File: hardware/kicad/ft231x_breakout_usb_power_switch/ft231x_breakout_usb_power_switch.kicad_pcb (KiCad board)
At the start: 2 copper layers, 60 x 31.2 mm, 71 parts, among them J1 USB_B_Micro_ALT, J2 USB_A_ALT, J3 Conn_01x08, J4 Conn_01x06, J5 Conn_01x08, Q3 2N7002, SW1 B3U-1000P, U1 SRV05-4, U2 FT231XS, U3 TPS2553DBVR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

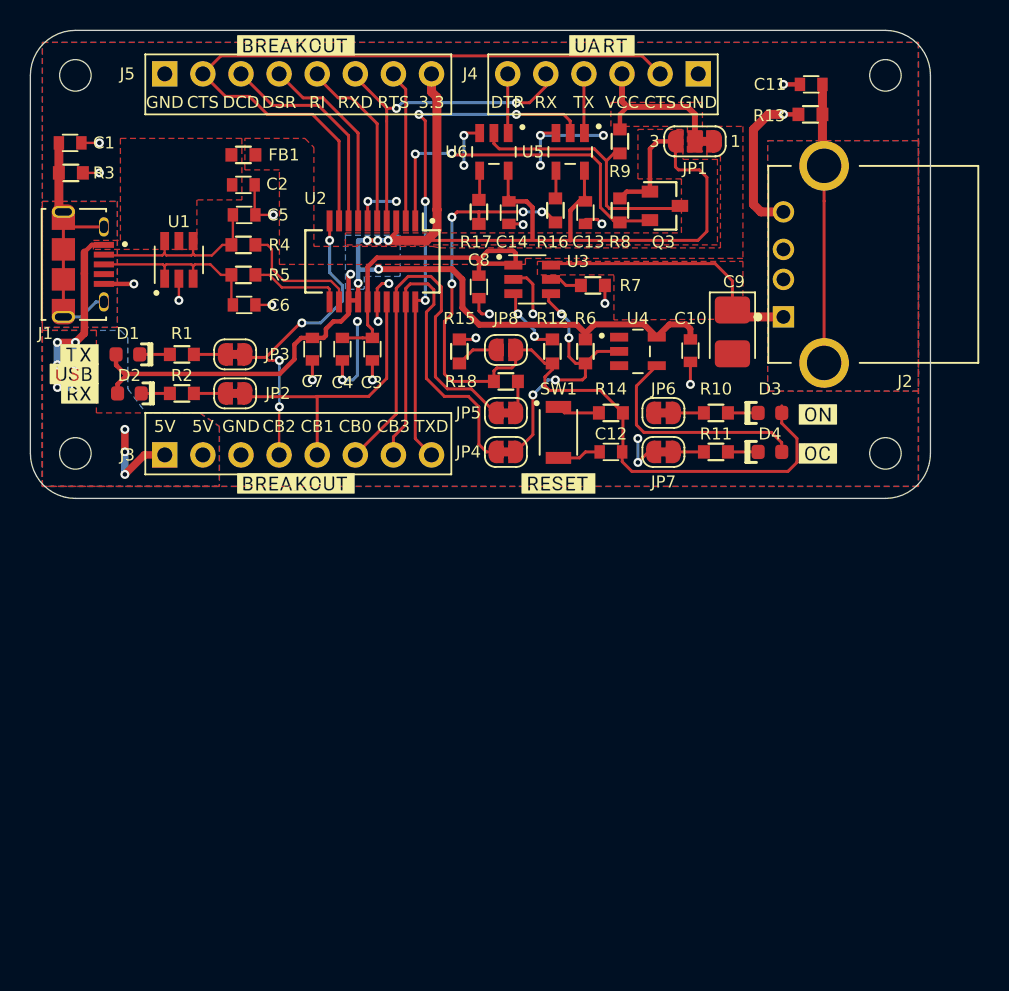
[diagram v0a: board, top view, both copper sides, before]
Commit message: Add two fiducials
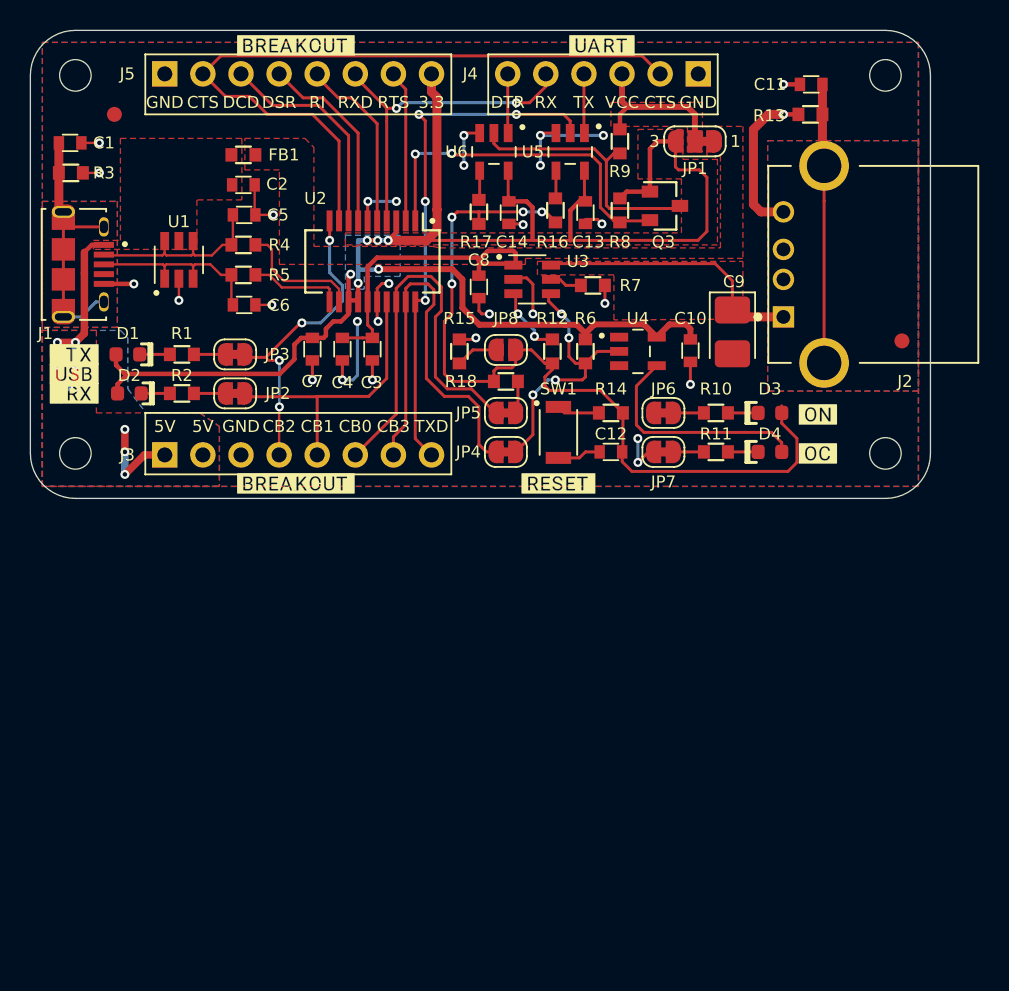
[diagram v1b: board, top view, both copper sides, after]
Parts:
- added FID1: Fiducial, -Mechanical:Fiducial_1mm_Mask2mm, F.Cu at (115.6, 75.0)
- added FID2: Fiducial, -Mechanical:Fiducial_1mm_Mask2mm, F.Cu at (168.1, 90.1)
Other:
- board text added: "VCC UART is 5V, to change to 3.3V cut JP1 pads 1 & 2 and bridge JP1 pads 2 & 3."
- board text removed: "VOUT UART is 5V, to change to 3.3V cut JP1 pads 1 & 2 and bridge JP1 pads 2 & 3."

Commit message: update resistor values in enable line
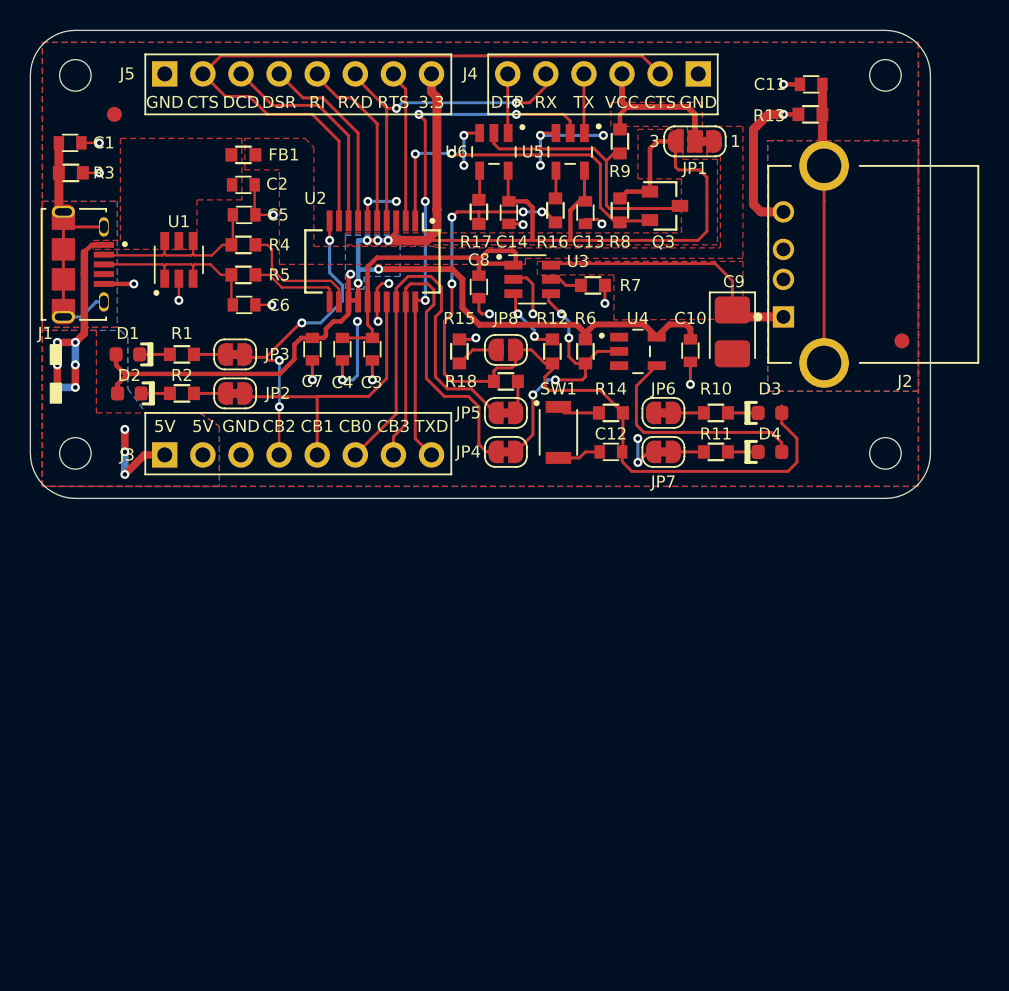
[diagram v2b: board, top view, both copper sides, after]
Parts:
- removed ? (x9): , buzzard_labels

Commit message: remove breakout headers and simplify
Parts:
- removed C14: 0.1uF, -Passive:C_0603
- removed J3: Conn_01x08, -Connector:PinHeader_1x08_P2.54mm_Vertical_CBUS
- removed J5: Conn_01x08, -Connector:PinHeader_1x08_P2.54mm_Vertical_CTS
- removed JP1: SolderJumper_3_Bridged12, -Switch:SolderJumper-3_P1.3mm_Bridged12_RoundedPad1.0x1.5mm_NumberLabels
- removed JP2, JP3, JP4, JP5, JP6, JP7: SolderJumper_2_Bridged_Alt, -Switch:SolderJumper-2_P1.3mm_Bridged_RoundedPad1.0x1.5mm
- removed Q3: 2N7002, -Chip:SOT-23-3
- removed R12, R16, R17: 1k, -Passive:R_0603
- removed R8, R9: 10k, -Passive:R_0603
- removed U6: NC7SZ66M5X, -Chip:SOT-23-5
- J4: value Conn_01x06 -> Conn_01x04; footprint -Connector:PinHeader_1x06_P2.54mm_Vertical_Arduino -> -Connector:PinHeader_1x04_P2.54mm_Vertical_Arduino
- R15: value 1k -> 10k
- R18: value 10k -> 1k
- moved J4 15.6 mm to (139.1, 74.8)
- moved U5 3.90 mm to (143.5, 80.5)
- moved D1 1.40 mm to (117.9, 91.0)
- moved D2 1.40 mm to (118.0, 93.6)
- moved R1 1.40 mm to (121.5, 91.0)
- moved R2 1.40 mm to (121.5, 93.6)
- moved C13 0.55 mm to (147.0, 81.0), turned to 90 degrees
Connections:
- net +5V renamed Net-(C3-Pad1)
- net VBUS renamed Net-(C2-Pad1)
- J4 pad 1: GND -> +3V3
- J4 pad 2: /CTS -> /STXD
- J4 pad 3: /VOUT -> /RXD
- J4 pad 4: /STXD -> GND
- R1 pad 1: Net-(JP3-Pad1) -> /TXLED
- R10 pad 1: Net-(JP6-Pad1) -> GND
- R11 pad 2: Net-(JP7-Pad1) -> GND
- R18 pad 2: Net-(JP5-Pad1) -> /GPO
- R2 pad 1: Net-(JP2-Pad1) -> /RXLED
- U2 pad 1: /DTR -> Net-(U2-Pad1)
- U2 pad 19: /GPI -> /FAULT
- U2 pad 2: /RTS -> Net-(U2-Pad2)
- U2 pad 5: /RI -> Net-(U2-Pad5)
- U2 pad 7: /DSR -> Net-(U2-Pad7)
- U2 pad 8: /DCD -> Net-(U2-Pad8)
- U2 pad 9: /CTS -> Net-(U2-Pad9)
- U3 pad 3: Net-(R12-Pad2) -> /EN
- U5 pad 4: Net-(R16-Pad2) -> /EN
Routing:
- net /CTS: track 47.9 -> 0.00 mm
- net +3V3: track 117.7 -> 86.2 mm
- net /GPI: track 28.4 -> 0.00 mm
- net /DTR: track 23.3 -> 0.00 mm, vias 2 -> 0
- net Net-(C2-Pad1): track 22.4 -> 0.00 mm, vias 9 -> 0
- net /TXD: track 35.1 -> 15.6 mm, vias 4 -> 2
- net /RES: track 18.2 -> 0.00 mm
- net /RXD: track 22.6 -> 7.37 mm, vias 2 -> 0
- net /DCD: track 14.7 -> 0.00 mm
- net /FAULT: track 18.1 -> 31.1 mm
- net /DSR: track 12.9 -> 0.00 mm
- net /RI: track 11.9 -> 0.00 mm
- net /VOUT: track 11.3 -> 0.00 mm
- net GND: track 64.8 -> 54.1 mm, vias 30 -> 23
- net /RTS: track 10.1 -> 0.00 mm
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- removed copper zone on F.Cu, net /VOUT
- removed copper zone on B.Cu, net Net-(C2-Pad1)
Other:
- board text removed: "VCC UART is 5V, to change to 3.3V cut JP1 pads 1 & 2 and bridge JP1 pads 2 & 3."

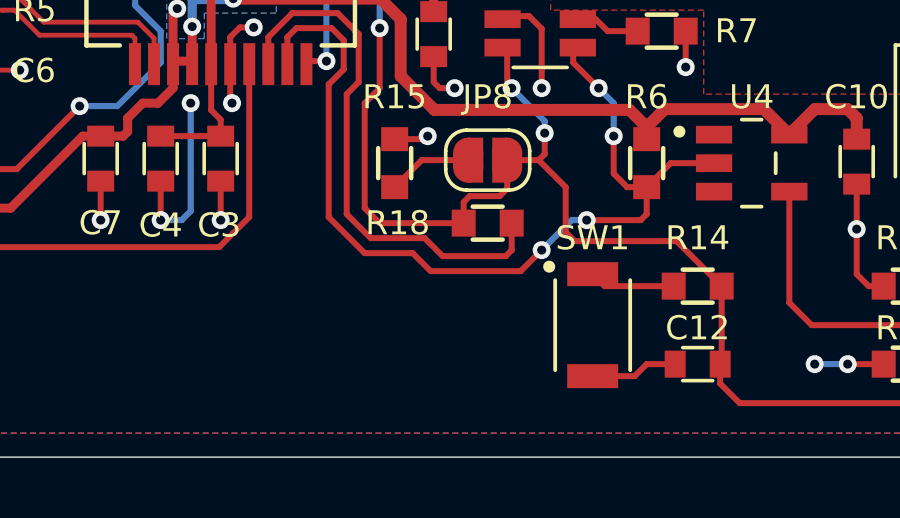
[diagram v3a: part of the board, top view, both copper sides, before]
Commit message: change to larger tactile switch
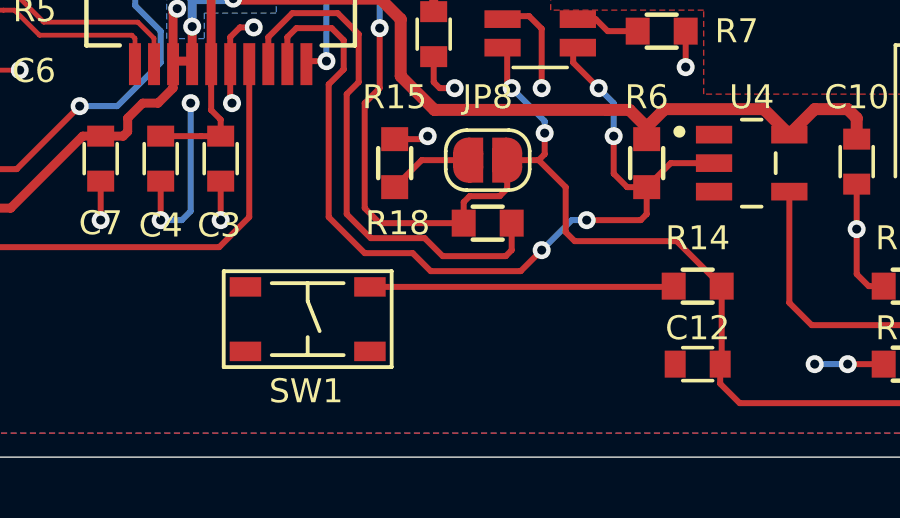
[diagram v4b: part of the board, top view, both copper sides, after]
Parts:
- SW1: value B3U-1000P -> PTS810SJK250SMTRLFS; footprint -Switch:B3U-1000P -> -Switch:PTS810SJK250SMTRLFS-TACT4.2MM
- moved SW1 9.50 mm to (135.7, 96.0), turned to 180 degrees
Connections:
- SW1 pad 1: Net-(R14-Pad1) -> GND
- SW1 pad 2: GND -> Net-(SW1-Pad2)
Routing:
- net Net-(R14-Pad1): track 2.87 -> 10.2 mm
- net GND: track 54.1 -> 51.2 mm

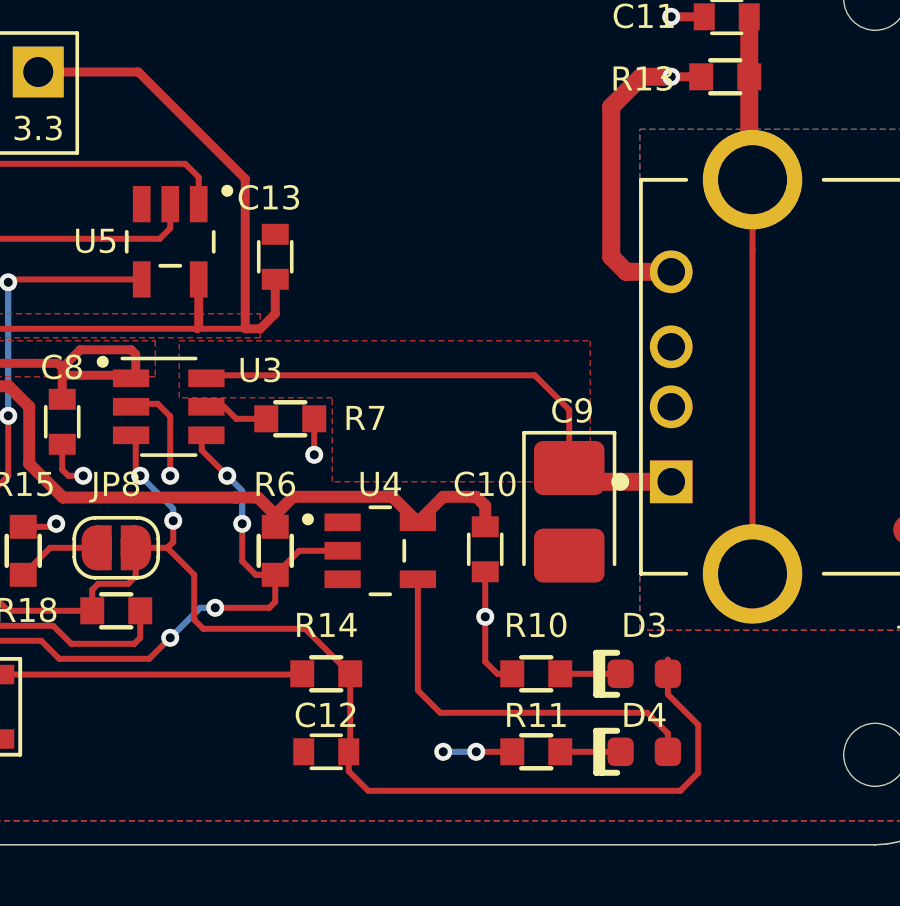
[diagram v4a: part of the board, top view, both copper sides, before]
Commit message: use buffer for on indicator
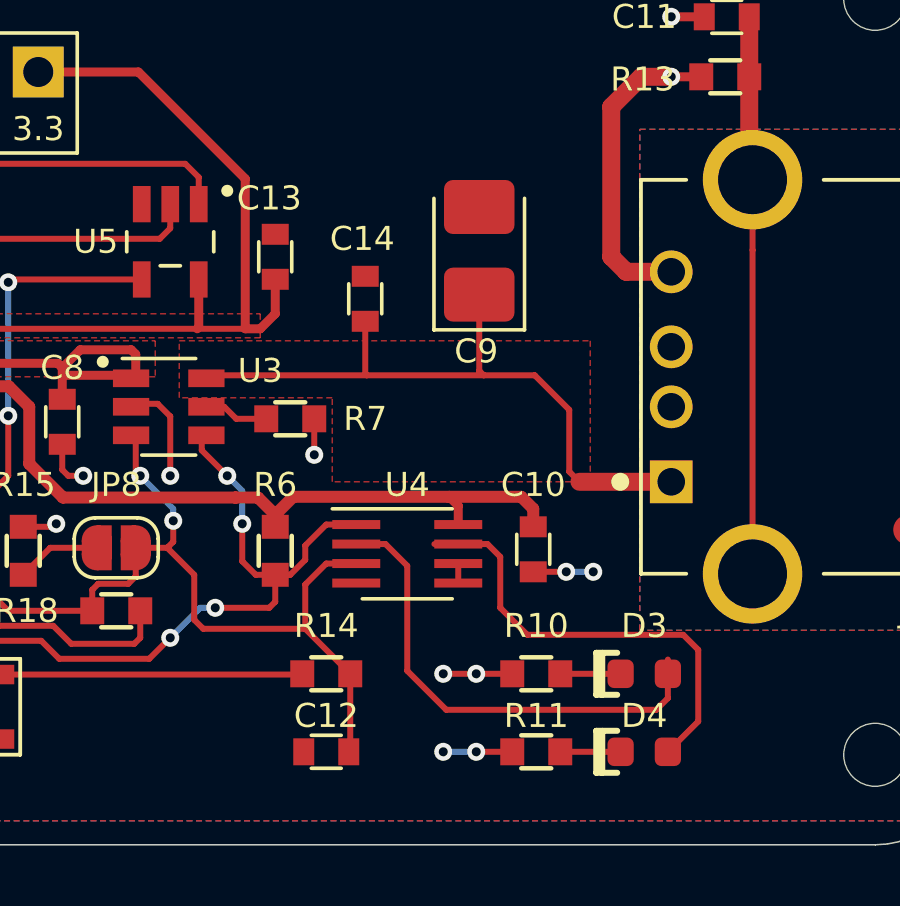
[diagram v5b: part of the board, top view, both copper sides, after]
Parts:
- added C14: 0.1uF, -Passive:C_0603, F.Cu at (150.0, 82.4)
- R18: value 1k -> 5k1
- U4: value SN74LVC1G04DBVR -> SN74LVC3G04DCTR; footprint -Chip:SOT-23-5 -> -Chip:SSOP-8_2.95x2.8mm_P0.65mm
- moved C9 9.20 mm to (153.8, 80.8), turned to 90 degrees
- moved C10 1.60 mm to (155.6, 90.8)
- moved U4 0.91 mm to (151.4, 90.9)
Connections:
- D3 pad 2: /EN -> Net-(D3-Pad2)
- U4 pad 1: Net-(U4-Pad1) -> /FAULT
- U4 pad 2: /FAULT -> Net-(D3-Pad2)
- U4 pad 3: GND -> /EN
- U4 pad 4: Net-(D4-Pad2) -> GND
- U4 pad 5: +3V3 -> /~EN
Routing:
- net Net-(D3-Pad2): track 0.00 -> 16.3 mm
- net /EN: track 56.0 -> 42.4 mm
- net Net-(C14-Pad1): track 18.8 -> 23.9 mm
- net +3V3: track 86.2 -> 88.0 mm
- net Net-(D4-Pad2): track 13.7 -> 15.5 mm
- net /FAULT: track 31.1 -> 32.2 mm
- net /~EN: track 0.00 -> 0.65 mm
- net GND: track 51.2 -> 51.4 mm, vias 23 -> 26
